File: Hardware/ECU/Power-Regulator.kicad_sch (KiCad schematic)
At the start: 22 parts, among them Q3 Q_PNP_BCEC, U15 MC33814, U16 TC4424A

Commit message: update to Kicad v9
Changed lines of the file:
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@@
 (kicad_sch
-	(version 20231120)
+	(version 20250114)
 	(generator "eeschema")
-	(generator_version "8.0")
+	(generator_version "9.0")
 	(paper "A4")
 	(junction

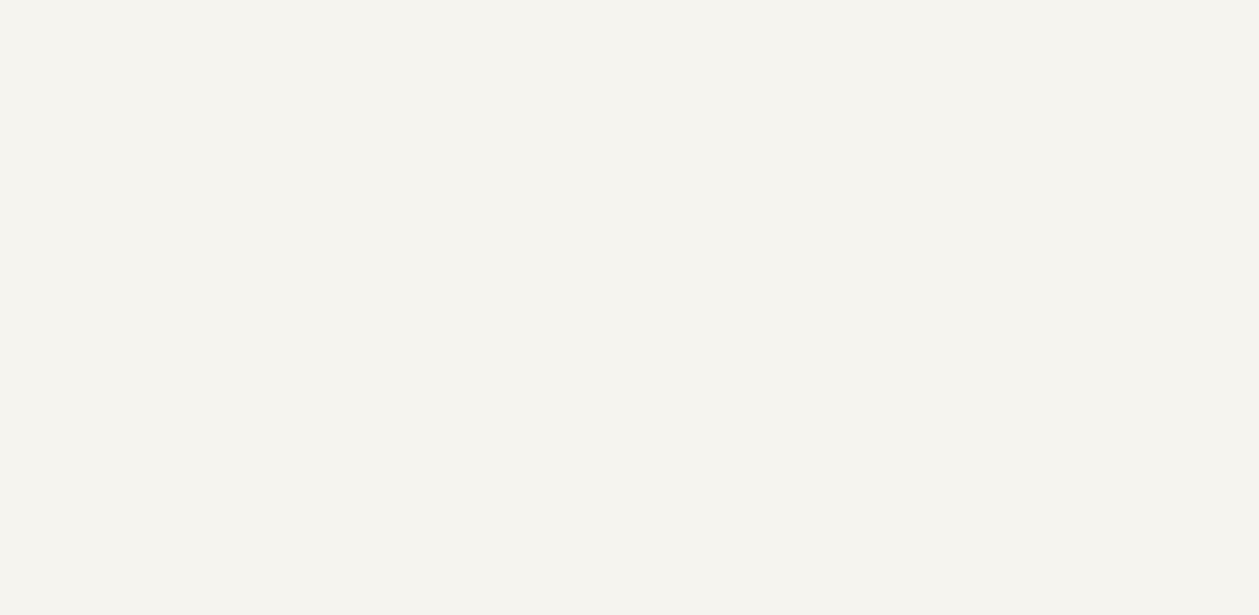
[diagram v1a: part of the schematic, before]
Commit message: Update 5V Supply
added TPS54202
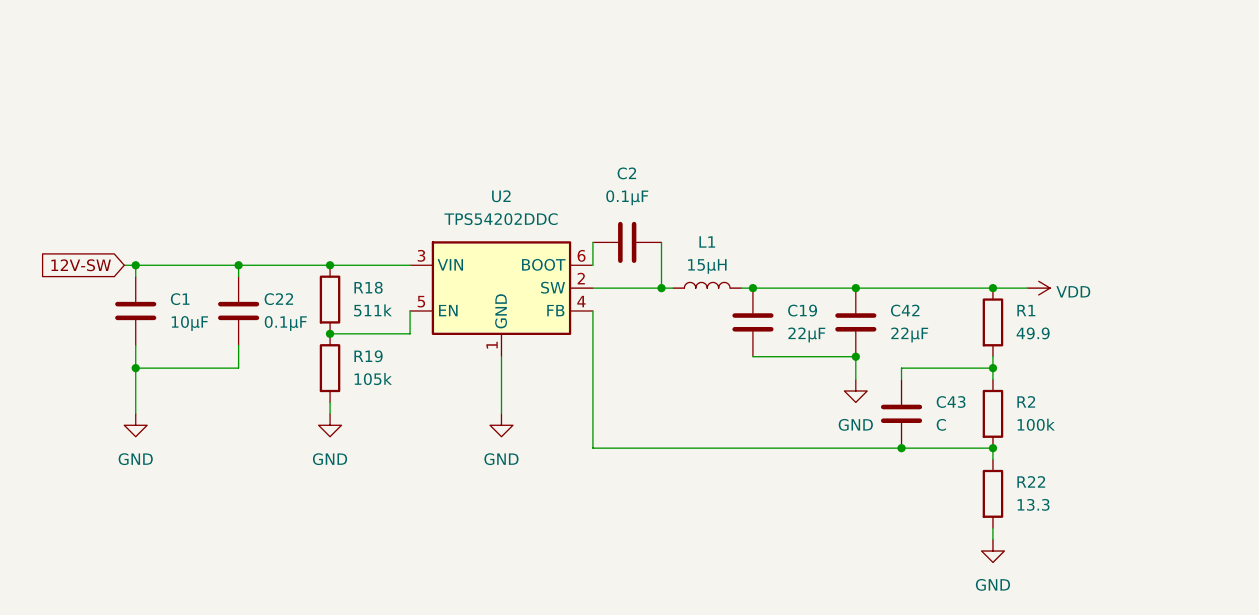
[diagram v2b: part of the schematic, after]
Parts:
- added C1: 10µF, symbol Device:C
- added C19, C42: 22µF, symbol Device:C
- added C2, C22: 0.1µF, symbol Device:C
- added C43: C, symbol Device:C
- added L1: 15µH, symbol Device:L
- added R1: 49.9, symbol Device:R
- added R18: 511k, symbol Device:R
- added R19: 105k, symbol Device:R
- added R2: 100k, symbol Device:R
- added R22: 13.3, symbol Device:R
- added U2: TPS54202DDC, Package_TO_SOT_SMD:SOT-23-6, symbol Regulator_Switching:TPS54202DDC
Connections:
- net +5V: now also C19.1, C42.1, L1.2, R1.1
- net 12V-SW: now also C1.1, C22.1, R18.1, U2.3 (VIN)
- net GND: now also C1.2, C19.2, C22.2, C42.2, R19.2, R22.2, U2.1 (GND)
- new net: C2.2, L1.1, U2.2 (SW)
- new net: C43.2, R2.2, R22.1, U2.4 (FB)
- new net: R18.2, R19.1, U2.5 (EN)
- new net: C2.1, U2.6 (BOOT)
- new net: C43.1, R1.2, R2.1

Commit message: modified:   Hardware/ECU/Drivers.kicad_sch 	deleted:    Hardware/ECU/ECU-backups/ECU-2025-05-15_143348.zip 	deleted:    Hardware/ECU/ECU-backups/ECU-2025-05-15_144355.zip 	deleted:    Hardware/ECU/ECU-backups/ECU-2025-05-15_152109.zip 	deleted:    Hardware/ECU/ECU-backups/ECU-2025-05-15_161628.zip 	deleted:    Hardware/ECU/ECU-backups/ECU-2025-05-15_162311.zip 	deleted:    Hardware/ECU/ECU-backups/ECU-2025-05-16_191516.zip 	deleted:    Hardware/ECU/ECU-backups/ECU-2025-05-16_192518.zip 	deleted:    Hardware/ECU/ECU-backups/ECU-2025-05-16_193610.zip 	new file:   Hardware/ECU/ECU-backups/ECU-2025-05-20_084251.zip 	new file:   Hardware/ECU/ECU-backups/ECU-2025-05-20_085713.zip 	new file:   Hardware/ECU/ECU-backups/ECU-2025-05-20_090304.zip 	new file:   Hardware/ECU/ECU-backups/ECU-2025-05-20_142748.zip 	new file:   Hardware/ECU/ECU-backups/ECU-2025-05-20_150003.zip 	new file:   Hardware/ECU/ECU-backups/ECU-2025-05-27_131057.zip 	new file:   Hardware/ECU/ECU-backups/ECU-2025-05-27_141528.zip 	new file:   Hardware/ECU/ECU-backups/ECU-2025-05-27_154948.zip 	new file:   Hardware/ECU/ECU-backups/ECU-2025-05-27_155558.zip 	new file:   Hardware/ECU/ECU.csv 	modified:   Hardware/ECU/ECU.kicad_pcb 	modified:   Hardware/ECU/ECU.kicad_pcb.zip 	new file:   Hardware/ECU/ECU.xml 	modified:   Hardware/ECU/Power-Regulator.kicad_sch 	modified:   Hardware/ECU/docs/Pinout.ods 	modified:   Hardware/ECU/fp-info-cache 	modified:   Hardware/ECU/fp-lib-table 	new file:   Hardware/ECU/lib/CRCW060349K9FKEAC.step 	new file:   Hardware/ECU/lib/CRCW060349K9FKEAC.wrl 	new file:   Hardware/ECU/lib/GRM21BC81A226ME44L.step 	new file:   Hardware/ECU/lib/GRM21BC81A226ME44L.wrl 	new file:   Hardware/ECU/lib/SamacSys_Parts.3dshapes/NE555DR.stp 	new file:   Hardware/ECU/lib/SamacSys_Parts.dcm 	new file:   Hardware/ECU/lib/SamacSys_Parts.kicad_sym 	new file:   Hardware/ECU/lib/SamacSys_Parts.lib 	new file:   Hardware/ECU/lib/SamacSys_Parts.mod 	new file:   Hardware/ECU/lib/SamacSys_Parts.pretty/NE555DR.kica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
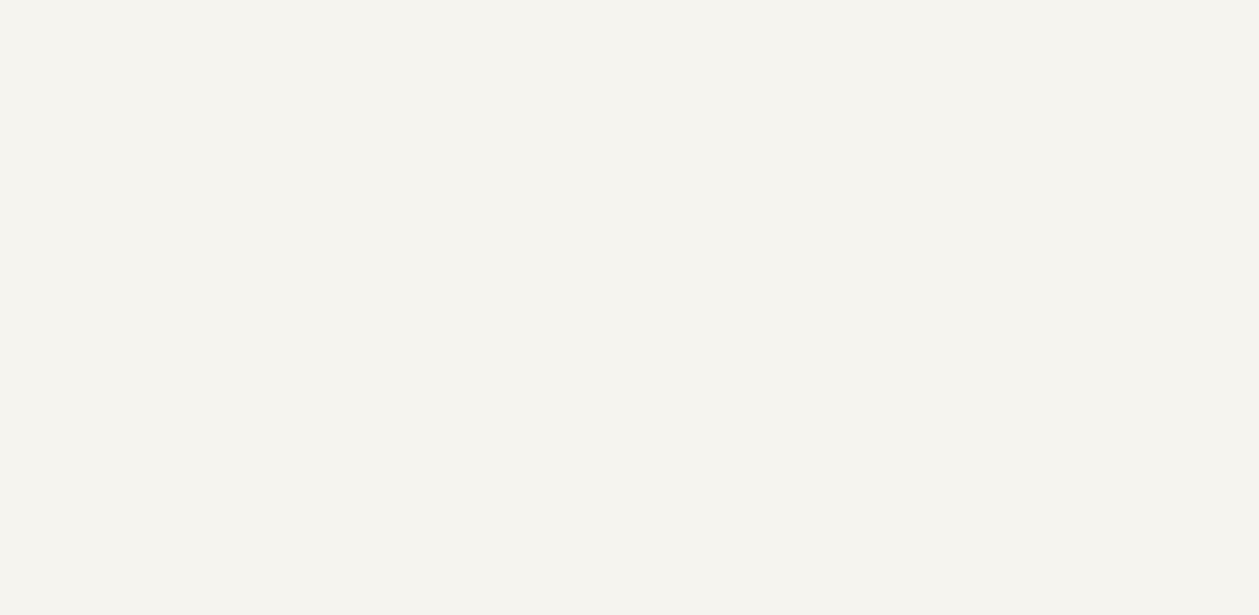
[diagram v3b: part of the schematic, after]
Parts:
- removed C1: 10µF, symbol Device:C
- removed C19, C42: 22µF, symbol Device:C
- removed C2, C22: 0.1µF, symbol Device:C
- removed C43: C, symbol Device:C
- removed L1: 15µH, symbol Device:L
- removed R1: 49.9, symbol Device:R
- removed R18: 511k, symbol Device:R
- removed R19: 105k, symbol Device:R
- removed R2: 100k, symbol Device:R
- removed R22: 13.3, symbol Device:R
- removed U2: TPS54202DDC, Package_TO_SOT_SMD:SOT-23-6, symbol Regulator_Switching:TPS54202DDC
